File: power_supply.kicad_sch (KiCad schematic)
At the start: 18 parts, among them J1 Разъём к автомобилю 2x16 (32 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, U6 MC78M05CDTG, U7 AMS1117-3.3

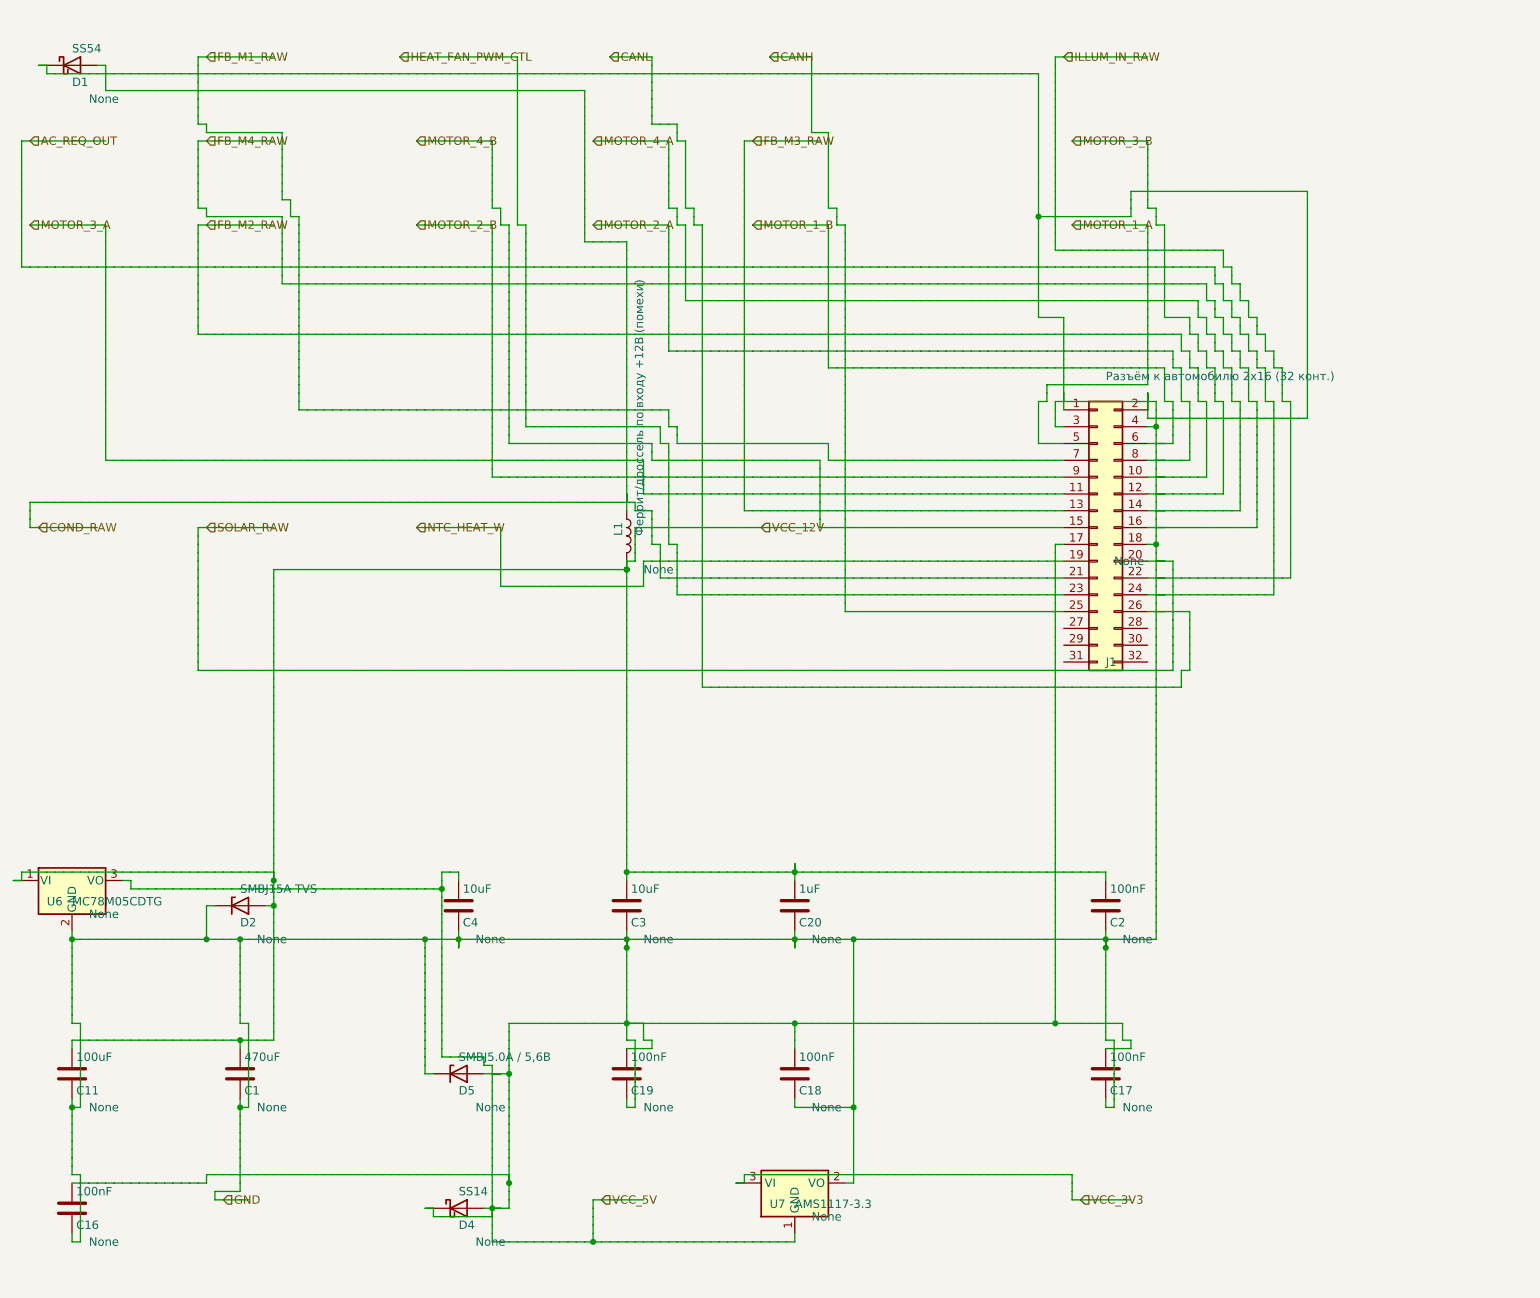
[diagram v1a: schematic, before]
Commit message: fix router map cell no more mark for pins
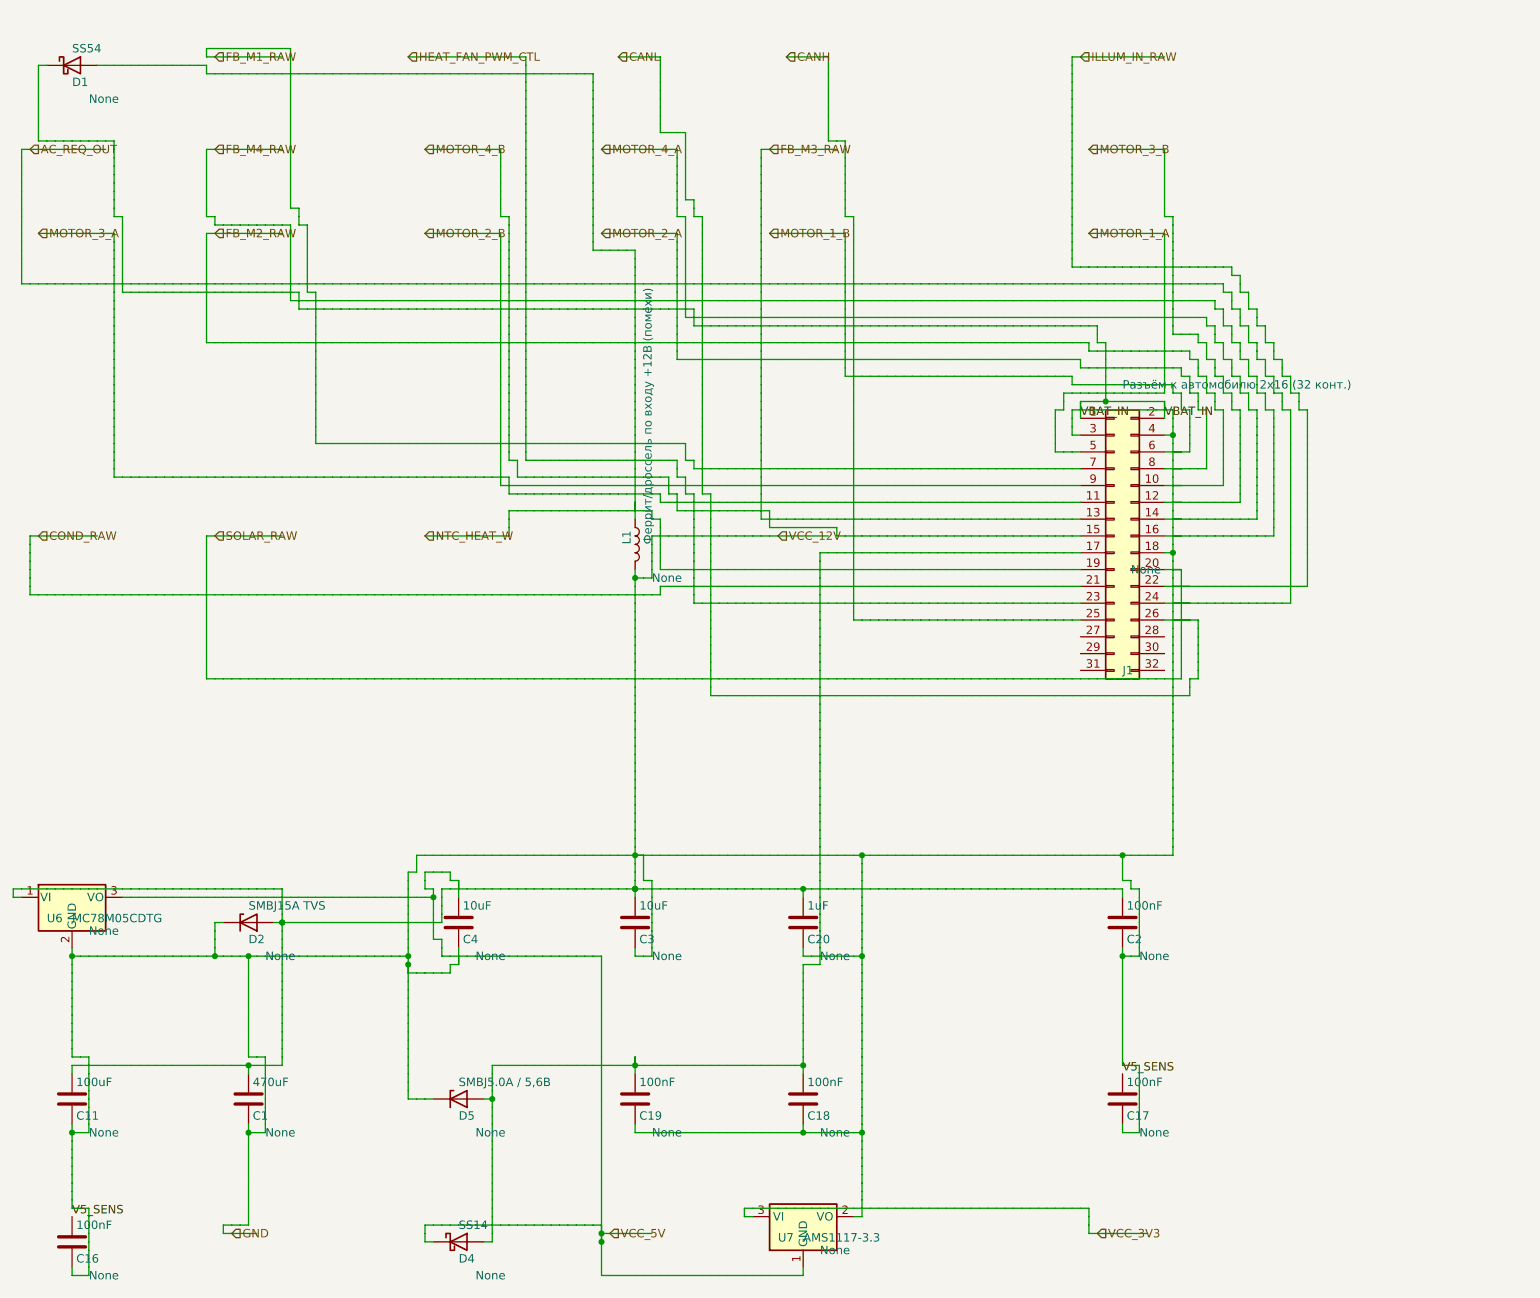
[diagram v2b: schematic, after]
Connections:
- net AC_REQ_OUT: no longer C16.1, C17.1
- new net V5_SENS: C16.1, C17.1

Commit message: рефакторинг проекта и начала прогона тестов
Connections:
- net V5_SENS is gone; now on net AC_REQ_OUT: C16.1, C17.1

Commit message: fix writer
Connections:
- net AC_REQ_OUT: no longer C1.1, C1.2, C11.1, C11.2, C16.1, C16.2, C17.1, C17.2, C18.1, C18.2, C19.1, C19.2, C2.1, C2.2, C20.1, C20.2, C3.1, C3.2, C4.1, C4.2, D1.1 (K), D1.2 (A), D2.1 (K), D2.2 (A), D4.1 (K), D4.2 (A), D5.1 (K), D5.2 (A), J1.1 (Pin_1), J1.10 (Pin_10), J1.11 (Pin_11), J1.12 (Pin_12), J1.13 (Pin_13), J1.14 (Pin_14), J1.15 (Pin_15), J1.16 (Pin_16), J1.17 (Pin_17), J1.18 (Pin_18), J1.19 (Pin_19), J1.2 (Pin_2), J1.20 (Pin_20), J1.21 (Pin_21), J1.22 (Pin_22), J1.23 (Pin_23), J1.25 (Pin_25), J1.26 (Pin_26), J1.3 (Pin_3), J1.4 (Pin_4), J1.5 (Pin_5), J1.6 (Pin_6), J1.7 (Pin_7), J1.8 (Pin_8), J1.9 (Pin_9), L1.1, L1.2, U6.1 (VI), U6.2 (GND), U6.3 (VO), U7.1 (GND), U7.2 (VO), U7.3 (VI)
- new net: C16.1, C17.1, C18.1, C19.1, D4.2 (A), D5.2 (A), J1.17 (Pin_17)
- new net: D1.2 (A), L1.1
- new net: D1.1 (K), J1.1 (Pin_1), J1.2 (Pin_2)
- new net CANH: J1.25 (Pin_25)
- new net CANL: J1.26 (Pin_26)
- new net COND_RAW: J1.21 (Pin_21)
- new net FB_M1_RAW: J1.7 (Pin_7)
- new net FB_M2_RAW: J1.10 (Pin_10)
- new net FB_M3_RAW: J1.13 (Pin_13)
- new net FB_M4_RAW: J1.16 (Pin_16)
- new net GND: C1.1, C1.2, C11.1, C11.2, C16.2, C17.2, C18.2, C19.2, C2.1, C2.2, C20.1, C20.2, C3.1, C3.2, C4.1, C4.2, D2.1 (K), D2.2 (A), D4.1 (K), D5.1 (K), J1.18 (Pin_18), J1.3 (Pin_3), J1.4 (Pin_4), L1.2, U6.1 (VI), U6.2 (GND), U6.3 (VO), U7.1 (GND), U7.2 (VO)
- new net HEAT_FAN_PWM_CTL: J1.23 (Pin_23)
- new net ILLUM_IN_RAW: J1.22 (Pin_22)
- new net MOTOR_1_A: J1.5 (Pin_5)
- new net MOTOR_1_B: J1.6 (Pin_6)
- new net MOTOR_2_A: J1.8 (Pin_8)
- new net MOTOR_2_B: J1.9 (Pin_9)
- new net MOTOR_3_A: J1.11 (Pin_11)
- new net MOTOR_3_B: J1.12 (Pin_12)
- new net MOTOR_4_A: J1.14 (Pin_14)
- new net MOTOR_4_B: J1.15 (Pin_15)
- new net NTC_HEAT_W: J1.19 (Pin_19)
- new net SOLAR_RAW: J1.20 (Pin_20)
- new net VCC_3V3: U7.3 (VI)

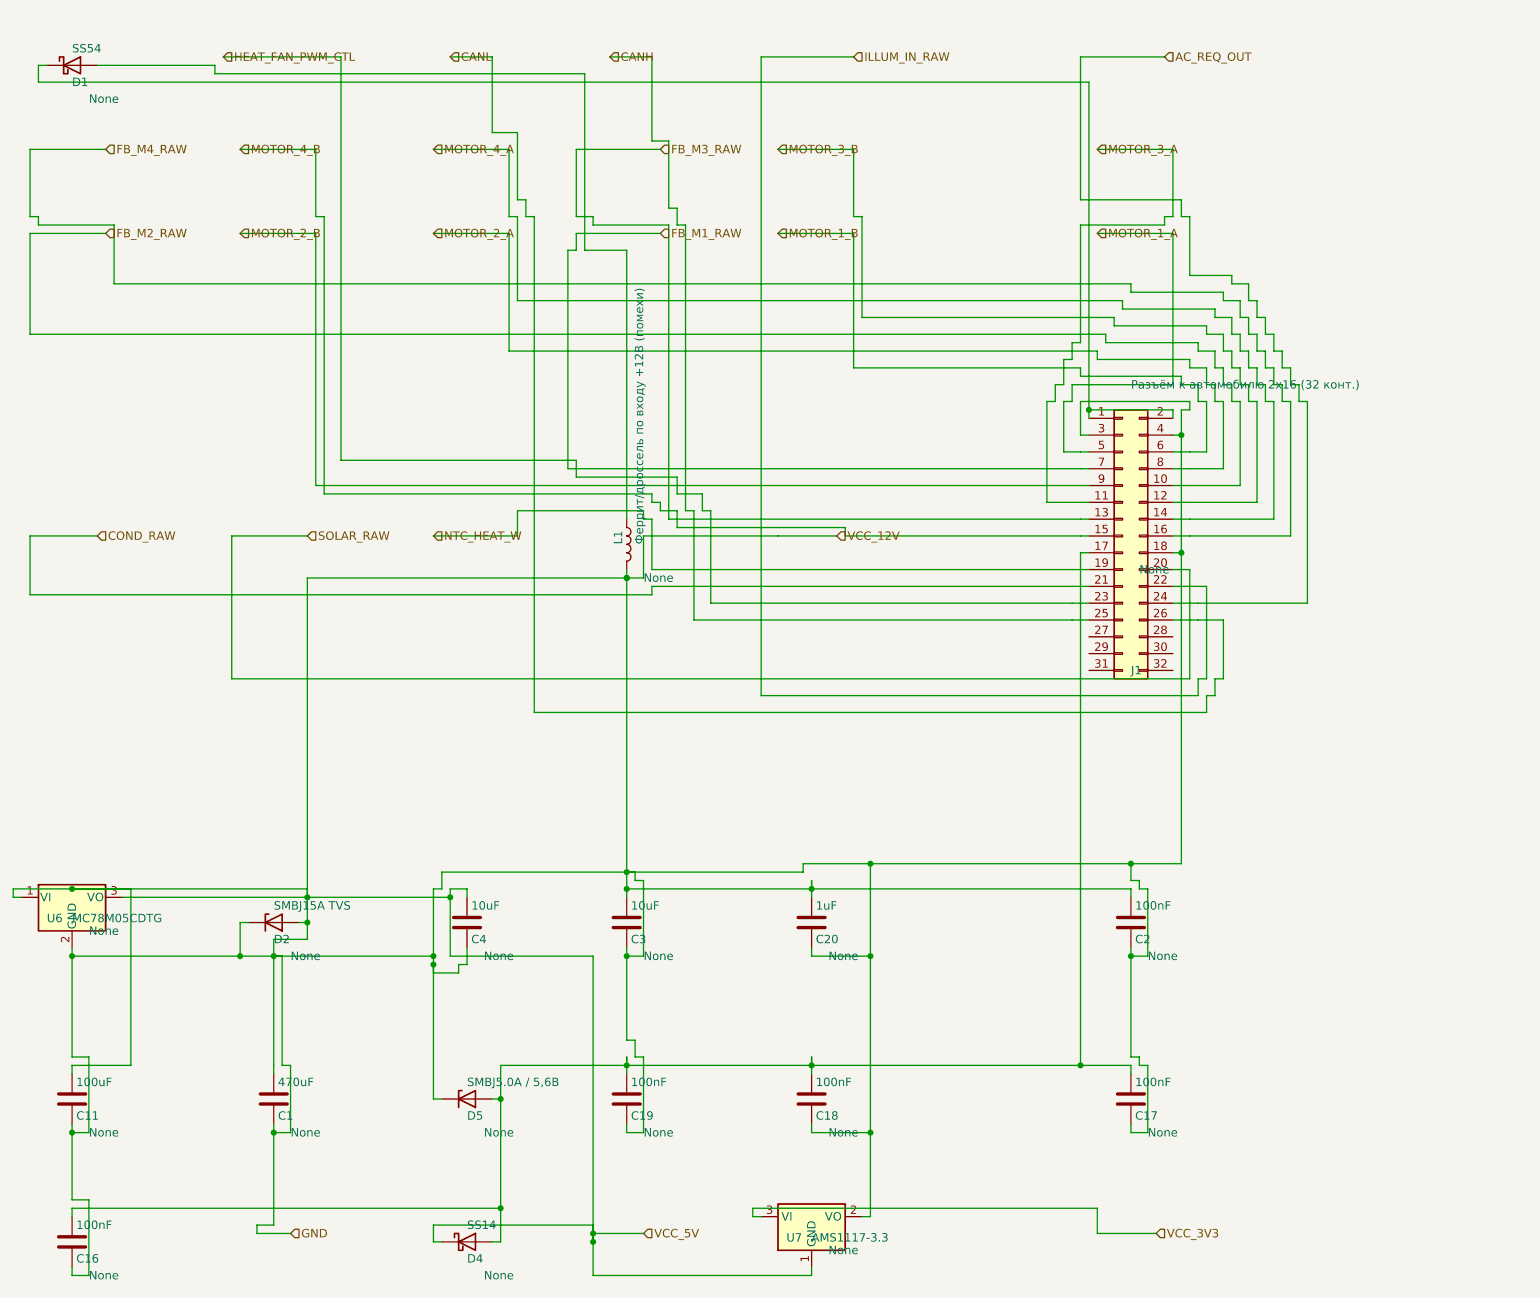
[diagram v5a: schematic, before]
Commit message: реализована 2я занятость клетки
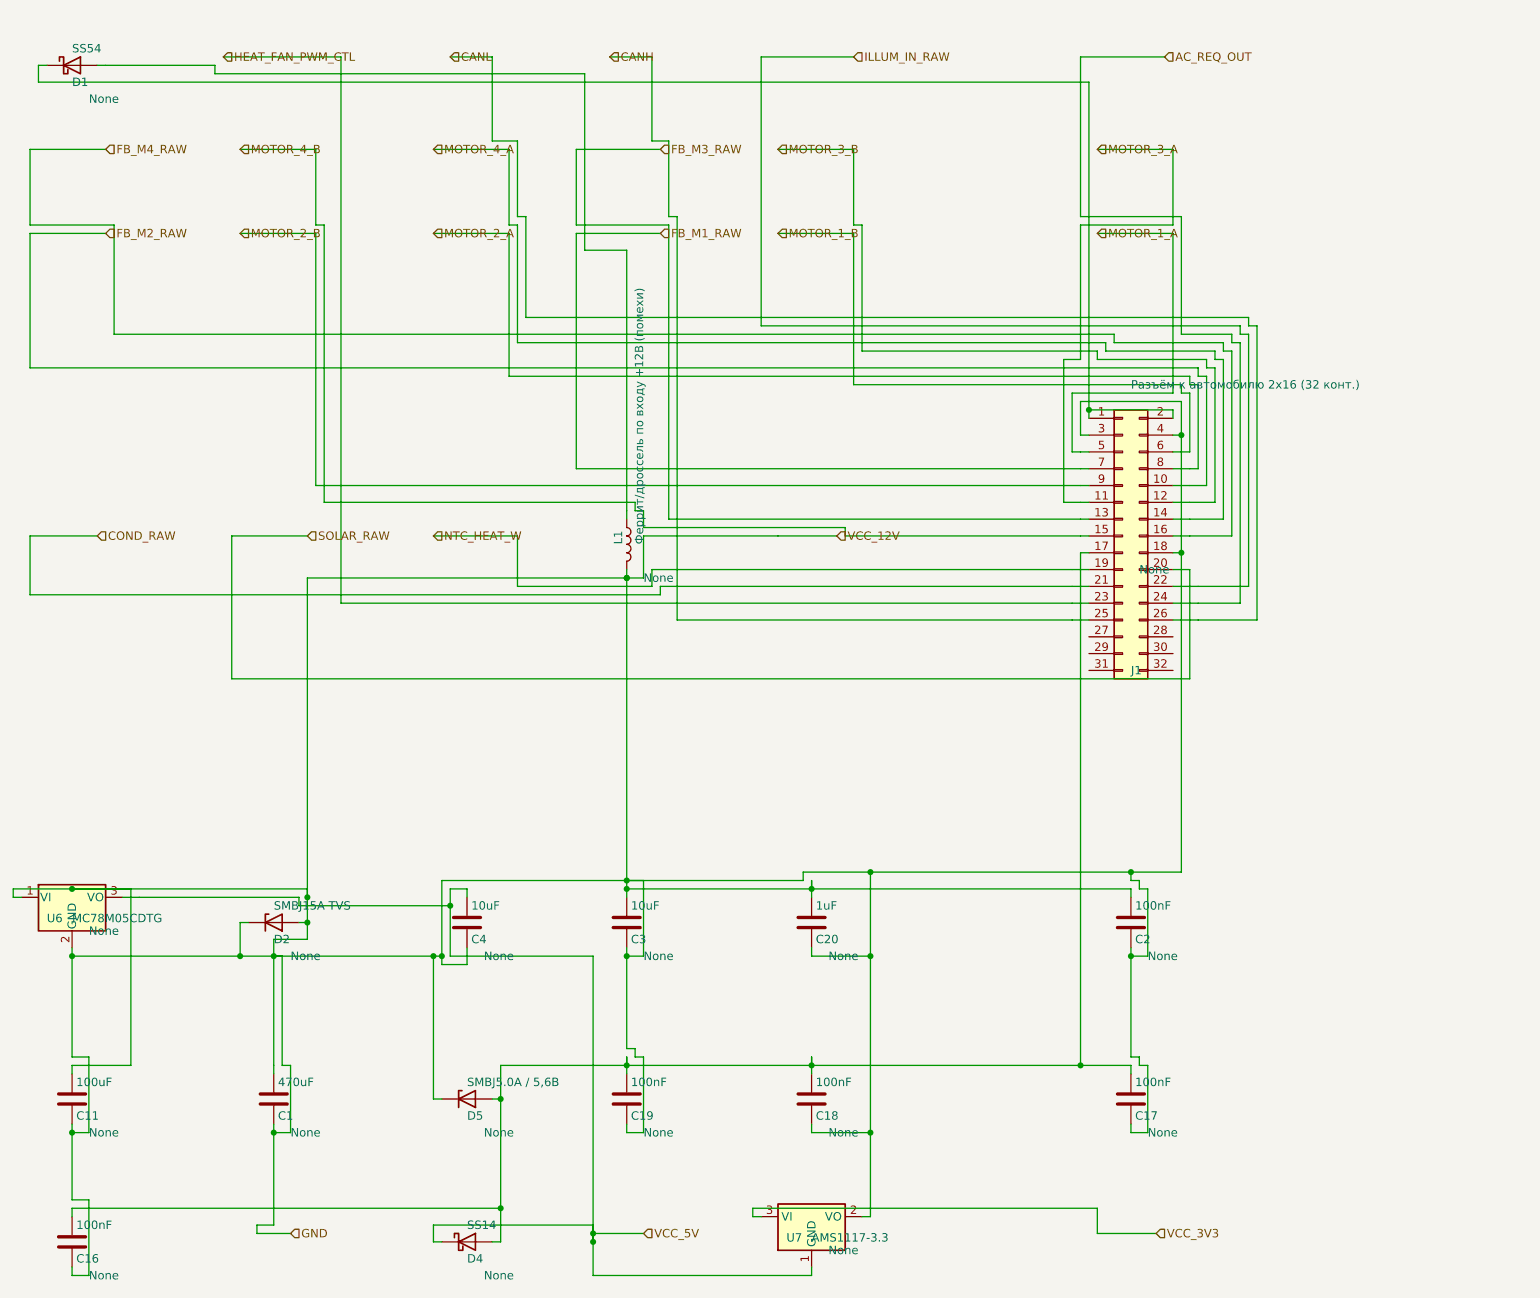
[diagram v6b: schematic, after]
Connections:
- net GND: no longer C4.1, D4.1 (K), U6.3 (VO), U7.1 (GND)
- new net VCC_5V: C4.1, D4.1 (K), U6.3 (VO), U7.1 (GND)
